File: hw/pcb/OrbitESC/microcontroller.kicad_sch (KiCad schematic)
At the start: 0 parts

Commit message: Start designing power stage
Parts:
- added J1: USB_C_Receptacle_USB2.0, symbol Connector:USB_C_Receptacle_USB2.0
- added J2: Micro_SD_Card_Det, symbol Connector:Micro_SD_Card_Det
- added U1: MCP2551-I-SN, Package_SO:SOIC-8_3.9x4.9mm_P1.27mm, symbol Interface_CAN_LIN:MCP2551-I-SN
- added U2: AT25SF081-SSHD-X, Package_SO:SOIC-8_3.9x4.9mm_P1.27mm, symbol Memory_Flash:AT25SF081-SSHD-X
- added U3: 24LC128, symbol Memory_EEPROM:24LC128
- added U4: STM32F446ZCHx, Package_BGA:UFBGA-144_7x7mm_Layout12x12_P0.5mm, symbol MCU_ST_STM32F4:STM32F446ZCHx
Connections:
- new net: J1.A1 (GND), J1.A12 (GND), J1.B1 (GND), J1.B12 (GND)
- new net: J1.A4 (VBUS), J1.A9 (VBUS), J1.B4 (VBUS), J1.B9 (VBUS)

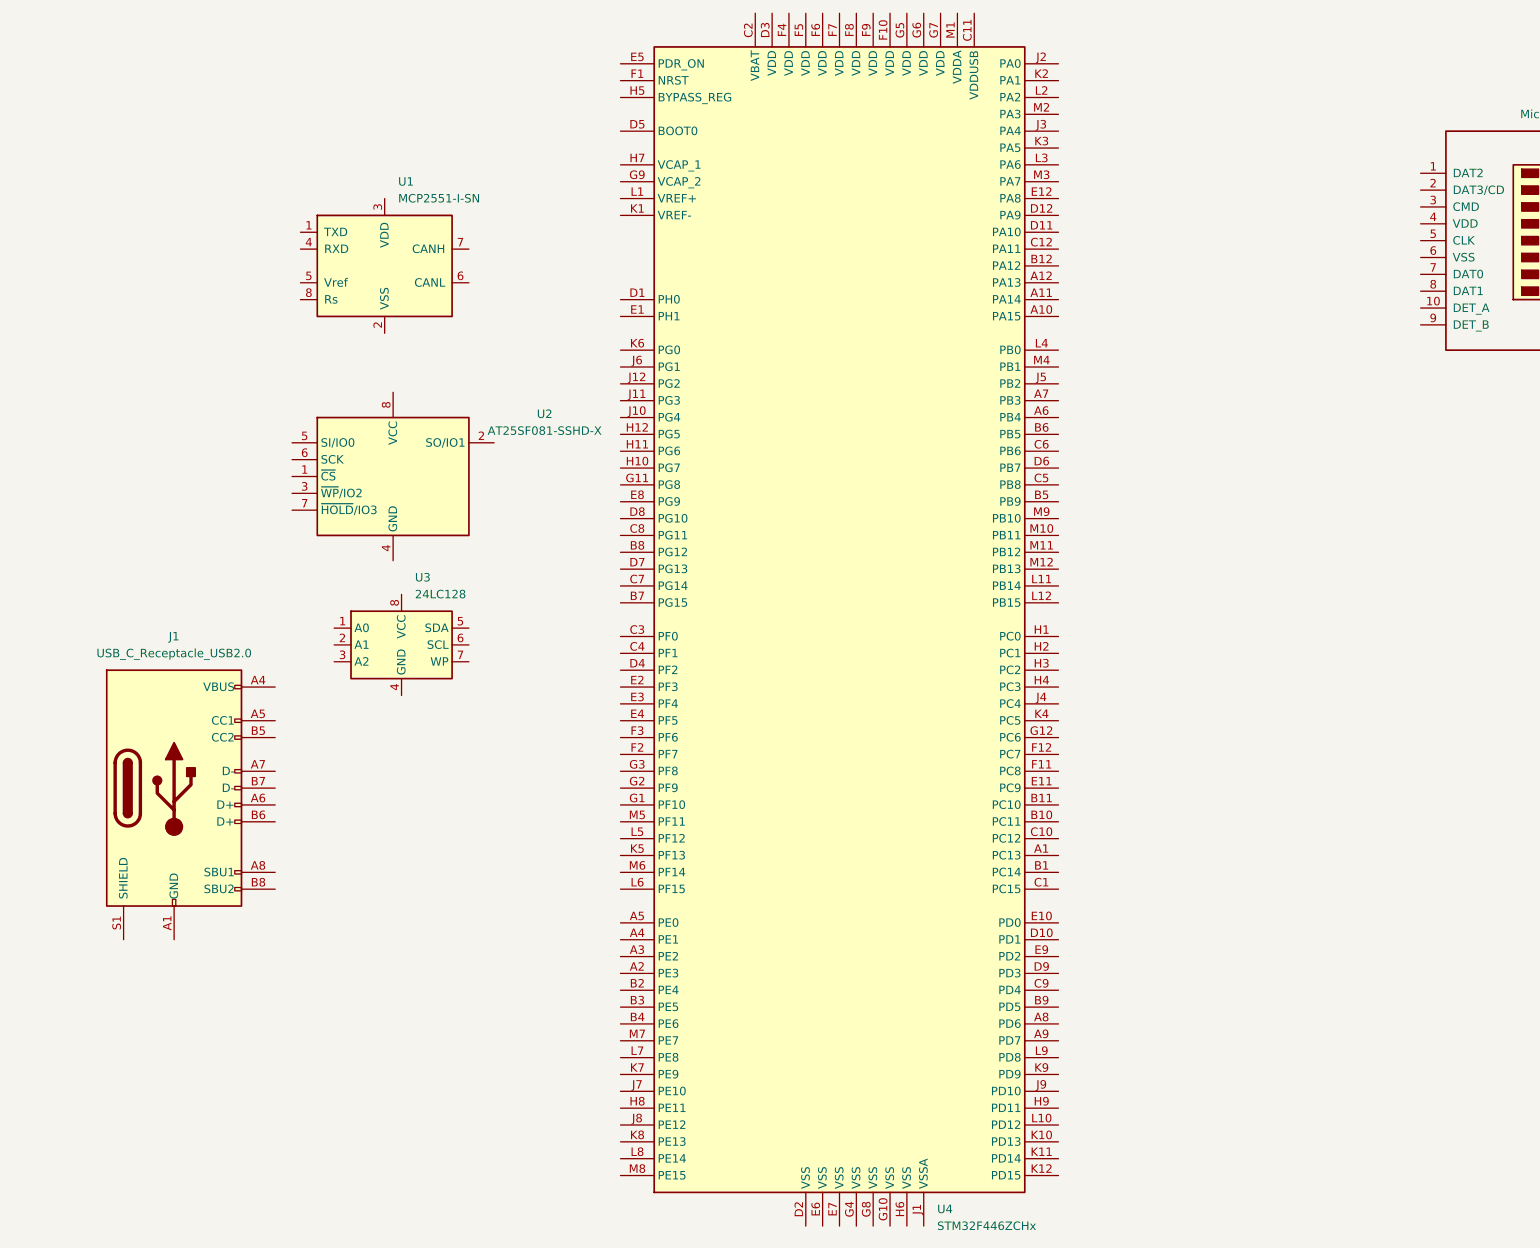
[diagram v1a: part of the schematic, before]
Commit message: Add power stage components
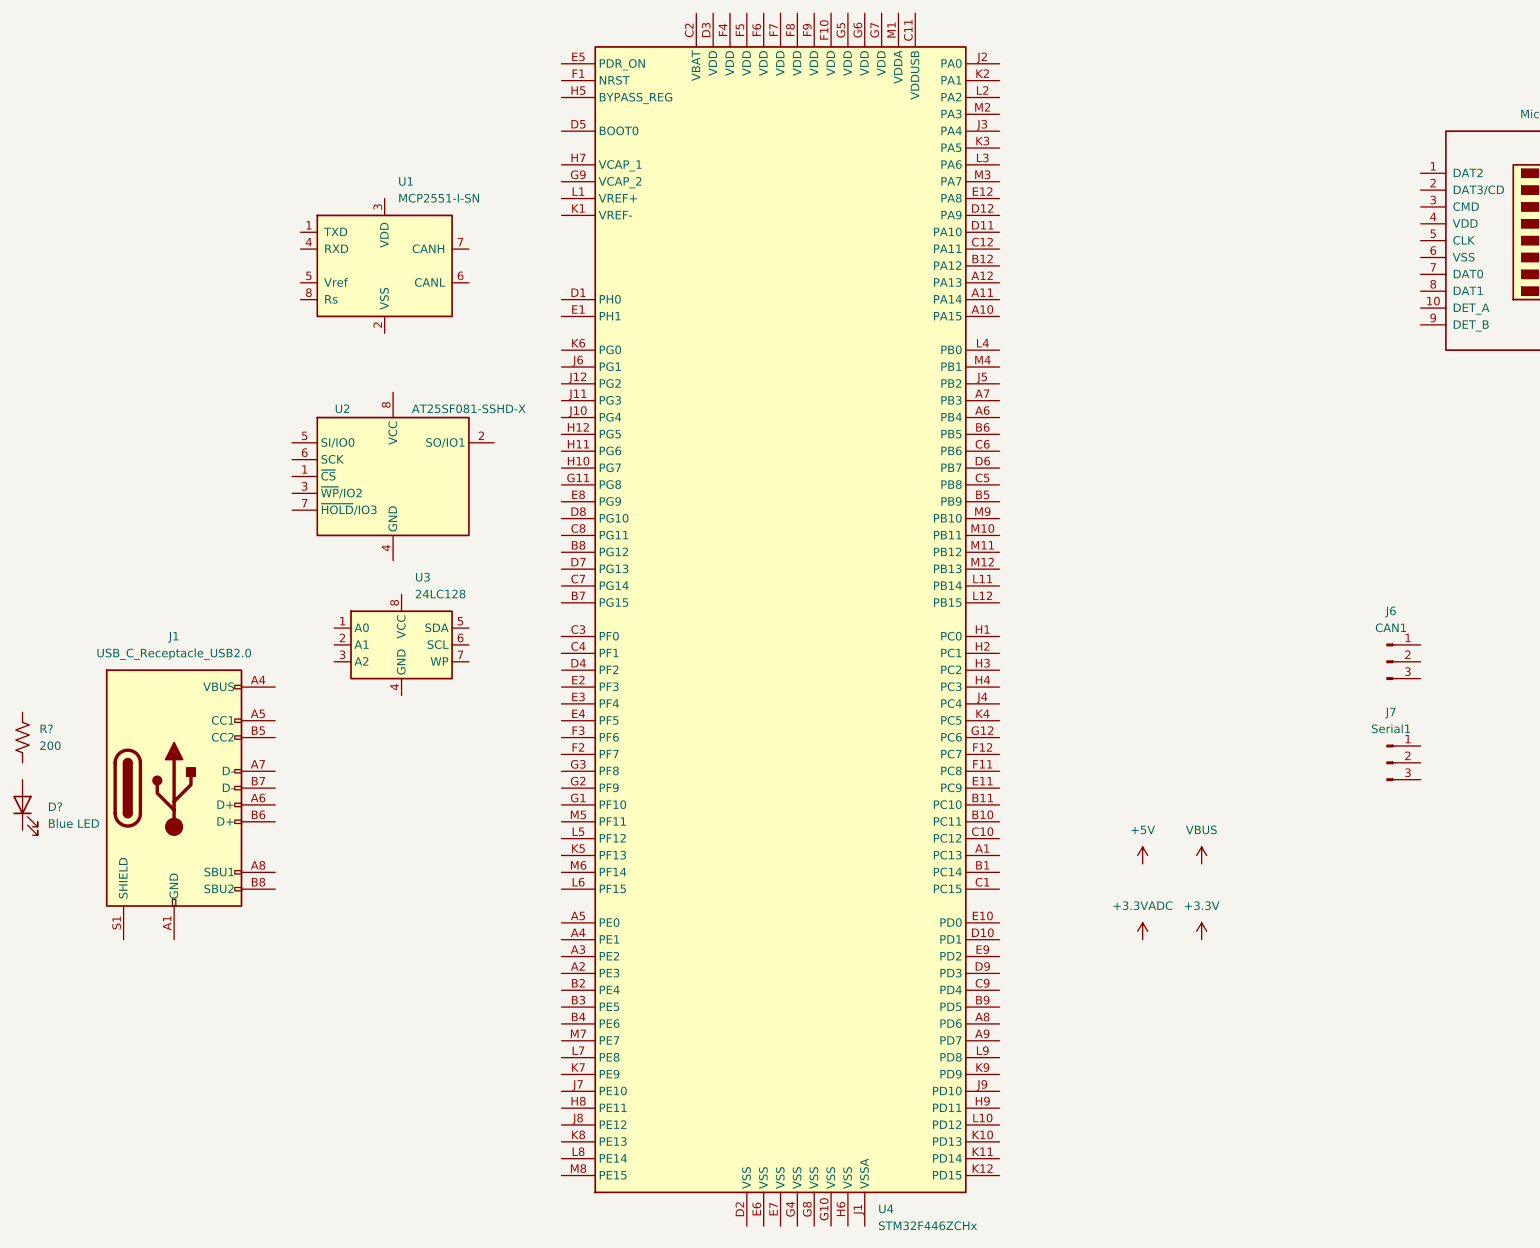
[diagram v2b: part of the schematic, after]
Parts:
- added D?: Blue LED, Diode_SMD:D_0603_1608Metric, symbol Device:LED
- added J6: CAN1, Connector_JST:JST_PH_B3B-PH-K_1x03_P2.00mm_Vertical, symbol Connector:Conn_01x03_Male
- added J7: Serial1, Connector_JST:JST_PH_B3B-PH-K_1x03_P2.00mm_Vertical, symbol Connector:Conn_01x03_Male
- added R?: 200, Resistor_SMD:R_0402_1005Metric, symbol Device:R_US
- J1: footprint (none) -> Connector_USB:USB_C_Receptacle_GCT_USB4085; DigiKey (none) -> 2073-USB4085-GF-ACT-ND
- J2: footprint (none) -> Connector_Card:microSD_HC_Molex_104031-0811; DigiKey (none) -> WM6357CT-ND
- U3: footprint (none) -> Package_SO:MSOP-8_3x3mm_P0.65mm
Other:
- moved on the sheet: U4
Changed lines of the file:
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@@
 (kicad_sch (version 20211123) (generator eeschema)
   (paper "A4")
+  (symbol (lib_id "power:+5V") (at 190.5 139.7 0) (unit 1)
+    (in_bom yes) (on_board yes) (fields_autoplaced)
+    (property "Reference" "#PWR?" (id 0) (at 190.5 143.51 0)
+      (effects (font (size 1.27 1.27)) hide)
+    )
+    (property "Value" "+5V" (id 1) (at 190.5 134.62 0))
+    (property "Footprint" "" (id 2) (at 190.5 139.7 0)
+      (effects (font (size 1.27 1.27)) hide)
+    )
+    (property "Datasheet" "" (id 3) (at 190.5 139.7 0)
+      (effects (font (size 1.27 1.27)) hide)
+    )
+    (pin "1")
+  )
+  (symbol (lib_id "power:+3.3V") (at 199.39 151.13 0) (unit 1)
+    (in_bom yes) (on_board yes) (fields_autoplaced)
+    (property "Reference" "#PWR?" (id 0) (at 199.39 154.94 0)
+      (effects (font (size 1.27 1.27)) hide)
+    )
+    (property "Value" "+3.3V" (id 1) (at 199.39 146.05 0))
+    (property "Footprint" "" (id 2) (at 199.39 151.13 0)
+      (effects (font (size 1.27 1.27)) hide)
+    )
+    (property "Datasheet" "" (id 3) (at 199.39 151.13 0)
+      (effects (font (size 1.27 1.27)) hide)
+    )
+    (pin "1")
+  )
+  (symbol (lib_id "Device:LED") (at 21.59 130.81 90) (unit 1)
+    (in_bom yes) (on_board yes) (fields_autoplaced)
+    (property "Reference" "D?" (id 0) (at 25.4 131.1274 90)
+      (effects (font (size 1.27 1.27)) (justify right))
+    )
+    (property "Value" "Blue LED" (id 1) (at 25.4 133.6674 90)
+      (effects (font (size 1.27 1.27)) (justify right))
+    )
+    (property "Footprint" "Diode_SMD:D_0603_1608Metric" (id 2) (at 21.59 130.81 0)
+      (effects (font (size 1.27 1.27)) hide)
+    )
+    (property "Datasheet" "https://datasheet.lcsc.com/lcsc/1811101510_Everlight-Elec-19-217-BHC-ZL1M2RY-3T_C72041.pdf" (id 3) (at 21.59 130.81 0)
+      (effects (font (size 1.27 1.27)) hide)
+    )
+    (property "JLCPCB" "C72041" (id 4) (at 21.59 130.81 90)
+      (effects (font (size 1.27 1.27)) hide)
+    )
+    (pin "1")
+    (pin "2")
+  )
   (symbol (lib_id "Connector:Micro_SD_Card_Det") (at 255.27 45.72 0) (unit 1)
     (in_bom yes) (on_board yes) (fields_autoplaced)
     (property "Reference" "J2" (id 0) (at 255.905 24.13 0))
     (property "Value" "Micro_SD_Card_Det" (id 1) (at 255.905 26.67 0))
-    (property "Footprint" "" (id 2) (at 307.34 27.94 0)
+    (property "Footprint" "Connector_Card:microSD_HC_Molex_104031-0811" (id 2) (at 307.34 27.94 0)
       (effects (font (size 1.27 1.27)) hide)
     )
     (property "Datasheet" "https://www.hirose.com/product/en/download_file/key_name/DM3/category/Catalog/doc_file_id/49662/?file_category_id=4&item_id=195&is_series=1" (id 3) (at 255.27 43.18 0)
+      (effects (font (size 1.27 1.27)) hide)
+    )
+    (property "DigiKey" "WM6357CT-ND" (id 4) (at 255.27 45.72 0)
       (effects (font (size 1.27 1.27)) hide)
     )
@@
     (property "Reference" "J1" (id 0) (at 44.45 105.41 0))
     (property "Value" "USB_C_Receptacle_USB2.0" (id 1) (at 44.45 107.95 0))
-    (property "Footprint" "" (id 2) (at 48.26 128.27 0)
+    (property "Footprint" "Connector_USB:USB_C_Receptacle_GCT_USB4085" (id 2) (at 48.26 128.27 0)
       (effects (font (size 1.27 1.27)) hide)
     )
     (property "Datasheet" "https://www.usb.org/sites/default/files/documents/usb_type-c.zip" (id 3) (at 48.26 128.27 0)
+      (effects (font (size 1.27 1.27)) hide)
+    )
+    (property "DigiKey" "2073-USB4085-GF-ACT-ND" (id 4) (at 44.45 128.27 0)
       (effects (font (size 1.27 1.27)) hide)
     )
@@
     (pin "8")
   )
-  (symbol (lib_id "MCU_ST_STM32F4:STM32F446ZCHx") (at 144.78 102.87 0) (unit 1)
-    (in_bom yes) (on_board yes) (fields_autoplaced)
-    (property "Reference" "U4" (id 0) (at 159.4994 191.77 0)
-      (effects (font (size 1.27 1.27)) (justify left))
-    )
-    (property "Value" "STM32F446ZCHx" (id 1) (at 159.4994 194.31 0)
-      (effects (font (size 1.27 1.27)) (justify left))
-    )
-    (property "Footprint" "Package_BGA:UFBGA-144_7x7mm_Layout12x12_P0.5mm" (id 2) (at 116.84 189.23 0)
+  (symbol (lib_id "MCU_ST_STM32F4:STM32F446ZCHx") (at 135.89 102.87 0) (unit 1)
+    (in_bom yes) (on_board yes) (fields_autoplaced)
+    (property "Reference" "U4" (id 0) (at 150.6094 191.77 0)
+      (effects (font (size 1.27 1.27)) (justify left))
+    )
+    (property "Value" "STM32F446ZCHx" (id 1) (at 150.6094 194.31 0)
+      (effects (font (size 1.27 1.27)) (justify left))
+    )
+    (property "Footprint" "Package_BGA:UFBGA-144_7x7mm_Layout12x12_P0.5mm" (id 2) (at 107.95 189.23 0)
       (effects (font (size 1.27 1.27)) (justify right) hide)
     )
-    (property "Datasheet" "http://www.st.com/st-web-ui/static/active/en/resource/technical/document/datasheet/DM00141306.pdf" (id 3) (at 144.78 102.87 0)
-      (effects (font (size 1.27 1.27)) hide)
-    )
-    (property "Digikey" "497-19011-ND" (id 4) (at 144.78 102.87 0)
+    (property "Datasheet" "http://www.st.com/st-web-ui/static/active/en/resource/technical/document/datasheet/DM00141306.pdf" (id 3) (at 135.89 102.87 0)
+      (effects (font (size 1.27 1.27)) hide)
+    )
+    (property "Digikey" "497-19011-ND" (id 4) (at 135.89 102.87 0)
       (effects (font (size 1.27 1.27)) hide)
     )
@@
       (effects (font (size 1.27 1.27)) (justify left))
     )
-    (property "Footprint" "" (id 2) (at 78.74 106.68 0)
+    (property "Footprint" "Package_SO:MSOP-8_3x3mm_P0.65mm" (id 2) (at 78.74 106.68 0)
       (effects (font (size 1.27 1.27)) hide)
     )
@@
   )
   (symbol (lib_id "Memory_Flash:AT25SF081-SSHD-X") (at 77.47 81.28 0) (unit 1)
-    (in_bom yes) (on_board yes) (fields_autoplaced)
-    (property "Reference" "U2" (id 0) (at 100.33 71.8693 0))
-    (property "Value" "AT25SF081-SSHD-X" (id 1) (at 100.33 74.4093 0))
+    (in_bom yes) (on_board yes)
+    (property "Reference" "U2" (id 0) (at 69.85 71.12 0))
+    (property "Value" "AT25SF081-SSHD-X" (id 1) (at 88.9 71.12 0))
     (property "Footprint" "Package_SO:SOIC-8_3.9x4.9mm_P1.27mm" (id 2) (at 77.47 96.52 0)
       (effects (font (size 1.27 1.27)) hide)
@@
     (pin "8")
   )
+  (symbol (lib_id "power:VBUS") (at 199.39 139.7 0) (unit 1)
+    (in_bom yes) (on_board yes) (fields_autoplaced)
+    (property "Reference" "#PWR?" (id 0) (at 199.39 143.51 0)
+      (effects (font (size 1.27 1.27)) hide)
+    )
+    (property "Value" "VBUS" (id 1) (at 199.39 134.62 0))
+    (property "Footprint" "" (id 2) (at 199.39 139.7 0)
+      (effects (font (size 1.27 1.27)) hide)
+    )
+    (property "Datasheet" "" (id 3) (at 199.39 139.7 0)
+      (effects (font (size 1.27 1.27)) hide)
+    )
+    (pin "1")
+  )
+  (symbol (lib_id "power:+3.3VADC") (at 190.5 151.13 0) (unit 1)
+    (in_bom yes) (on_board yes) (fields_autoplaced)
+    (property "Reference" "#PWR?" (id 0) (at 194.31 152.4 0)
+      (effects (font (size 1.27 1.27)) hide)
+    )
+    (property "Value" "+3.3VADC" (id 1) (at 190.5 146.05 0))
+    (property "Footprint" "" (id 2) (at 190.5 151.13 0)
+      (effects (font (size 1.27 1.27)) hide)
+    )
+    (property "Datasheet" "" (id 3) (at 190.5 151.13 0)
+      (effects (font (size 1.27 1.27)) hide)
+    )
+    (pin "1")
+  )
+  (symbol (lib_id "Connector:Conn_01x03_Male") (at 227.33 124.46 0) (unit 1)
+    (in_bom yes) (on_board yes) (fields_autoplaced)
+    (property "Reference" "J7" (id 0) (at 227.965 116.84 0))
+    (property "Value" "Serial1" (id 1) (at 227.965 119.38 0))
+    (property "Footprint" "Connector_JST:JST_PH_B3B-PH-K_1x03_P2.00mm_Vertical" (id 2) (at 227.33 124.46 0)
+      (effects (font (size 1.27 1.27)) hide)
+    )
+    (property "Datasheet" "~" (id 3) (at 227.33 124.46 0)
+      (effects (font (size 1.27 1.27)) hide)
+    )
+    (pin "1")
+    (pin "2")
+    (pin "3")
+  )
+  (symbol (lib_id "Device:R_US") (at 21.59 120.65 0) (unit 1)
+    (in_bom yes) (on_board yes) (fields_autoplaced)
+    (property "Reference" "R?" (id 0) (at 24.13 119.3799 0)
+      (effects (font (size 1.27 1.27)) (justify left))
+    )
+    (property "Value" "200" (id 1) (at 24.13 121.9199 0)
+      (effects (font (size 1.27 1.27)) (justify left))
+    )
+    (property "Footprint" "Resistor_SMD:R_0402_1005Metric" (id 2) (at 22.606 120.904 90)
+      (effects (font (size 1.27 1.27)) hide)
+    )
+    (property "Datasheet" "~" (id 3) (at 21.59 120.65 0)
+      (effects (font (size 1.27 1.27)) hide)
+    )
+    (property "JLCPCB" "C25087" (id 4) (at 21.59 120.65 0)
+      (effects (font (size 1.27 1.27)) hide)
+    )
+    (pin "1")
+    (pin "2")
+  )
+  (symbol (lib_id "Connector:Conn_01x03_Male") (at 227.33 109.22 0) (unit 1)
+    (in_bom yes) (on_board yes) (fields_autoplaced)
+    (property "Reference" "J6" (id 0) (at 227.965 101.6 0))
+    (property "Value" "CAN1" (id 1) (at 227.965 104.14 0))
+    (property "Footprint" "Connector_JST:JST_PH_B3B-PH-K_1x03_P2.00mm_Vertical" (id 2) (at 227.33 109.22 0)
+      (effects (font (size 1.27 1.27)) hide)
+    )
+    (property "Datasheet" "~" (id 3) (at 227.33 109.22 0)
+      (effects (font (size 1.27 1.27)) hide)
+    )
+    (pin "1")
+    (pin "2")
+    (pin "3")
+  )
 )

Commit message: Initial planning of MCU connections
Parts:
- added SW?: Break, Button_Switch_SMD:SW_SPST_PTS810, symbol Switch:SW_Push
- added SW?: Boot, Button_Switch_SMD:SW_SPST_PTS810, symbol Switch:SW_Push
- added SW?: Reset, Button_Switch_SMD:SW_SPST_PTS810, symbol Switch:SW_Push
- gave numbers to parts that had none: 2
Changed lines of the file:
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@@
   (symbol (lib_id "power:+5V") (at 190.5 139.7 0) (unit 1)
     (in_bom yes) (on_board yes) (fields_autoplaced)
-    (property "Reference" "#PWR?" (id 0) (at 190.5 143.51 0)
+    (property "Reference" "#PWR038" (id 0) (at 190.5 143.51 0)
       (effects (font (size 1.27 1.27)) hide)
     )
@@
     (pin "1")
   )
+  (symbol (lib_id "Switch:SW_Push") (at 229.87 82.55 0) (unit 1)
+    (in_bom yes) (on_board yes) (fields_autoplaced)
+    (property "Reference" "SW?" (id 0) (at 229.87 74.93 0))
+    (property "Value" "Break" (id 1) (at 229.87 77.47 0))
+    (property "Footprint" "Button_Switch_SMD:SW_SPST_PTS810" (id 2) (at 229.87 77.47 0)
+      (effects (font (size 1.27 1.27)) hide)
+    )
+    (property "Datasheet" "~" (id 3) (at 229.87 77.47 0)
+      (effects (font (size 1.27 1.27)) hide)
+    )
+    (pin "1")
+    (pin "2")
+  )
   (symbol (lib_id "power:+3.3V") (at 199.39 151.13 0) (unit 1)
     (in_bom yes) (on_board yes) (fields_autoplaced)
-    (property "Reference" "#PWR?" (id 0) (at 199.39 154.94 0)
+    (property "Reference" "#PWR041" (id 0) (at 199.39 154.94 0)
       (effects (font (size 1.27 1.27)) hide)
     )
@@
   (symbol (lib_id "Device:LED") (at 21.59 130.81 90) (unit 1)
     (in_bom yes) (on_board yes) (fields_autoplaced)
-    (property "Reference" "D?" (id 0) (at 25.4 131.1274 90)
+    (property "Reference" "D5" (id 0) (at 25.4 131.1274 90)
       (effects (font (size 1.27 1.27)) (justify right))
     )
@@
   (symbol (lib_id "power:VBUS") (at 199.39 139.7 0) (unit 1)
     (in_bom yes) (on_board yes) (fields_autoplaced)
-    (property "Reference" "#PWR?" (id 0) (at 199.39 143.51 0)
+    (property "Reference" "#PWR040" (id 0) (at 199.39 143.51 0)
       (effects (font (size 1.27 1.27)) hide)
     )
@@
   (symbol (lib_id "power:+3.3VADC") (at 190.5 151.13 0) (unit 1)
     (in_bom yes) (on_board yes) (fields_autoplaced)
-    (property "Reference" "#PWR?" (id 0) (at 194.31 152.4 0)
+    (property "Reference" "#PWR039" (id 0) (at 194.31 152.4 0)
       (effects (font (size 1.27 1.27)) hide)
     )
@@
     (pin "3")
   )
+  (symbol (lib_id "Switch:SW_Push") (at 208.28 95.25 0) (unit 1)
+    (in_bom yes) (on_board yes) (fields_autoplaced)
+    (property "Reference" "SW?" (id 0) (at 208.28 87.63 0))
+    (property "Value" "Boot" (id 1) (at 208.28 90.17 0))
+    (property "Footprint" "Button_Switch_SMD:SW_SPST_PTS810" (id 2) (at 208.28 90.17 0)
+      (effects (font (size 1.27 1.27)) hide)
+    )
+    (property "Datasheet" "~" (id 3) (at 208.28 90.17 0)
+      (effects (font (size 1.27 1.27)) hide)
+    )
+    (pin "1")
+    (pin "2")
+  )
   (symbol (lib_id "Device:R_US") (at 21.59 120.65 0) (unit 1)
     (in_bom yes) (on_board yes) (fields_autoplaced)
-    (property "Reference" "R?" (id 0) (at 24.13 119.3799 0)
+    (property "Reference" "R47" (id 0) (at 24.13 119.3799 0)
       (effects (font (size 1.27 1.27)) (justify left))
     )
@@
     (pin "3")
   )
+  (symbol (lib_id "Switch:SW_Push") (at 208.28 82.55 0) (unit 1)
+    (in_bom yes) (on_board yes) (fields_autoplaced)
+    (property "Reference" "SW?" (id 0) (at 208.28 74.93 0))
+    (property "Value" "Reset" (id 1) (at 208.28 77.47 0))
+    (property "Footprint" "Button_Switch_SMD:SW_SPST_PTS810" (id 2) (at 208.28 77.47 0)
+      (effects (font (size 1.27 1.27)) hide)
+    )
+    (property "Datasheet" "~" (id 3) (at 208.28 77.47 0)
+      (effects (font (size 1.27 1.27)) hide)
+    )
+    (pin "1")
+    (pin "2")
+  )
 )
